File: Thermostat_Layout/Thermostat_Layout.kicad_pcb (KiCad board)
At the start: 2 copper layers, 70 x 60 mm, 52 parts, among them J1 Conn_01x03, J2 Conn_01x02_Male, J3 LCD_HEADER, J4 Conn_Coaxial, J5 Conn_01x04, J6 Conn_01x10, SW1 SW_Push, U1 LM50CIM3, U10 TLP3545, U2 ATMEGA328P-AU, U3 TSR_1-2433, U4 MCP23S17_SO, U5 DS3231MZ, U6 nRF24L01P, U7 FM25V10, U8 TLP3545, U9 TLP3545, Y1 Crystal, Y2 16MHz

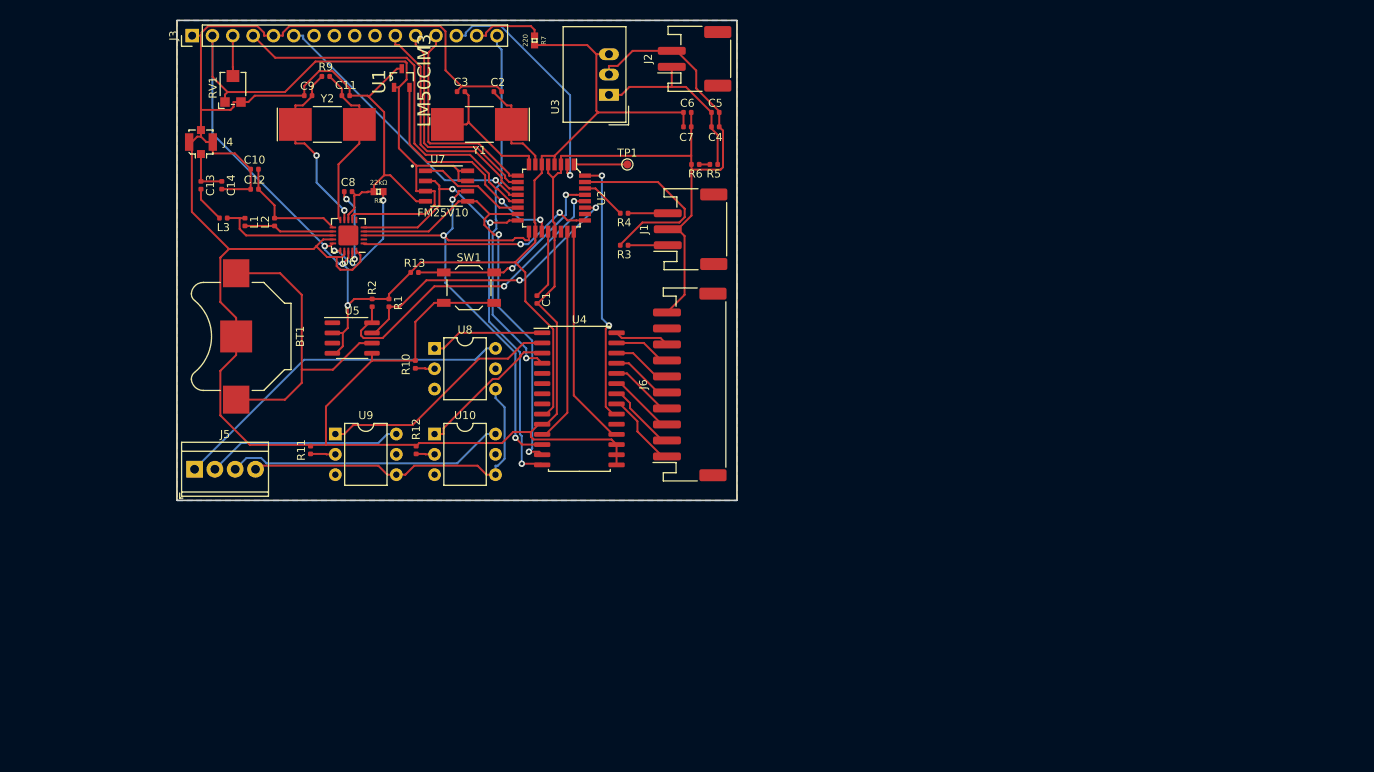
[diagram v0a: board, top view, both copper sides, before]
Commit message: Remove NRF24 from schematic
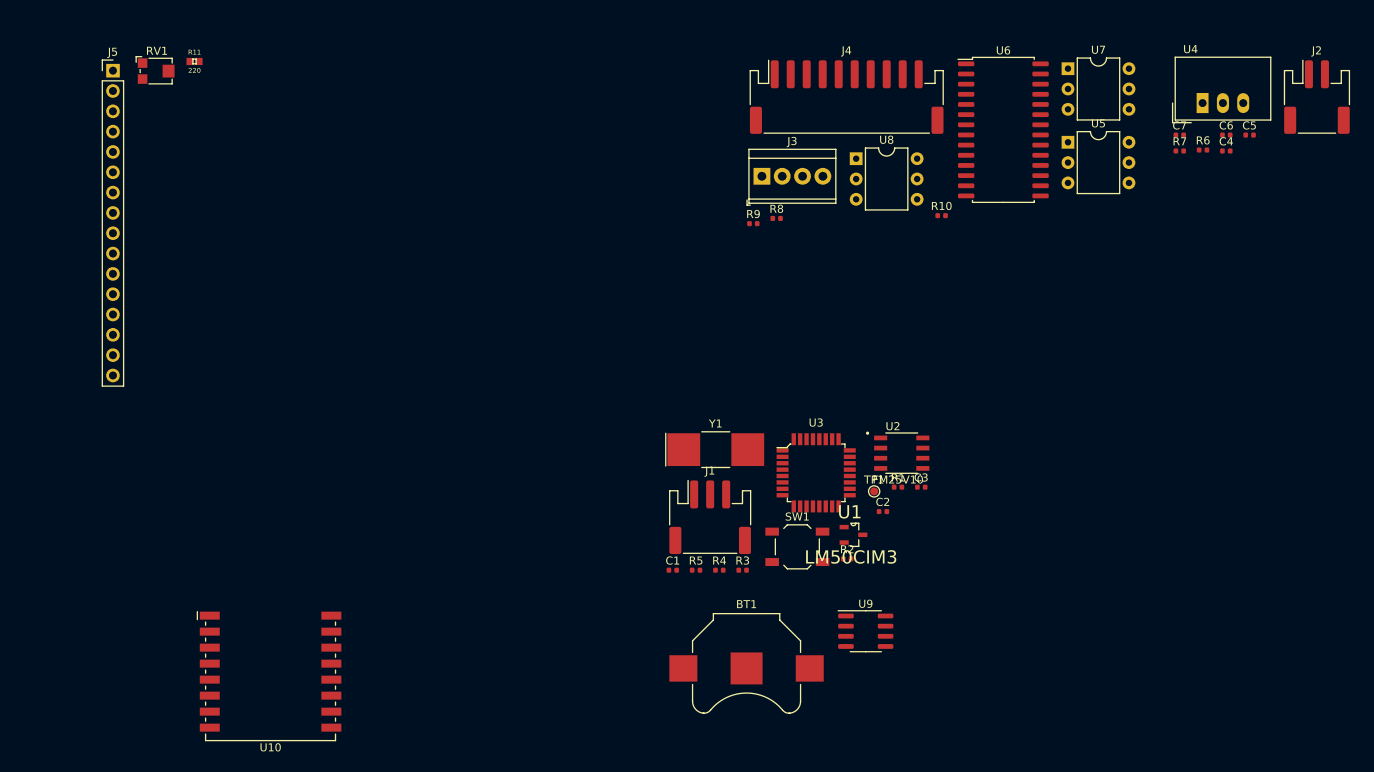
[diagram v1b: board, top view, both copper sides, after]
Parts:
- removed C10: 2.2nF, Capacitor_SMD:C_0402_1005Metric
- removed C11, C9: 22pF, Capacitor_SMD:C_0402_1005Metric
- removed C12: 4.7pF, Capacitor_SMD:C_0402_1005Metric
- removed C13: 15pF, Capacitor_SMD:C_0402_1005Metric
- removed C14: 1.5pF, Capacitor_SMD:C_0402_1005Metric
- removed C8: 33nF, Capacitor_SMD:C_0402_1005Metric
- removed J6: Conn_01x10, Connector_JST:JST_PH_S10B-PH-SM4-TB_1x10-1MP_P2.00mm_Horizontal
- removed L1: 12nH, Inductor_SMD:L_0402_1005Metric
- removed L2: 2.3nH, Inductor_SMD:L_0402_1005Metric
- removed L3: 7.9nH, Inductor_SMD:L_0402_1005Metric
- removed R12: 100Ω, Resistor_SMD:R_0402_1005Metric
- removed R13: 10kΩ, Resistor_SMD:R_0402_1005Metric
- removed Y2: 16MHz, Crystal:Crystal_SMD_SeikoEpson_MC405-2Pin_9.6x4.1mm
- C1: value 100nF -> 22pF
- C3: value 22pF -> 100nF
- J3: value LCD_HEADER -> Conn_01x04; footprint Connector_PinHeader_2.54mm:PinHeader_1x16_P2.54mm_Vertical -> TerminalBlock_TE-Connectivity:TerminalBlock_TE_282834-4_1x04_P2.54mm_Horizontal
- J4: value Conn_Coaxial -> Conn_01x10; footprint Connector_Coaxial:U.FL_Molex_MCRF_73412-0110_Vertical -> Connector_JST:JST_PH_S10B-PH-SM4-TB_1x10-1MP_P2.00mm_Horizontal
- J5: value Conn_01x04 -> LCD_HEADER; footprint TerminalBlock_TE-Connectivity:TerminalBlock_TE_282834-4_1x04_P2.54mm_Horizontal -> Connector_PinHeader_2.54mm:PinHeader_1x16_P2.54mm_Vertical
- R11: value 100Ω -> 220; footprint Resistor_SMD:R_0402_1005Metric -> Resistors:0402
- R3: value 1kΩ -> 10kΩ
- R5: value 220k -> 1kΩ
- R6: value 100k -> 220k
- R7: value 220 -> 100k; footprint Resistors:0402 -> Resistor_SMD:R_0402_1005Metric
- R8: value 22kΩ -> 100Ω; footprint Resistors:0402 -> Resistor_SMD:R_0402_1005Metric
- R9: value 1MΩ -> 100Ω
- U10: value TLP3545 -> ESP-07; footprint Package_DIP:DIP-6_W7.62mm -> RF_Module:ESP-07
- U2: value ATMEGA328P-AU -> FM25V10; footprint digikey-footprints:TQFP-32_7x7mm -> FM25V10:SOIC127P601X172-8N
- U3: value TSR_1-2433 -> ATMEGA328P-AU; footprint Converter_DCDC:Converter_DCDC_TRACO_TSR-1_THT -> digikey-footprints:TQFP-32_7x7mm
- U4: value MCP23S17_SO -> TSR_1-2433; footprint Package_SO:SOIC-28W_7.5x17.9mm_P1.27mm -> Converter_DCDC:Converter_DCDC_TRACO_TSR-1_THT
- U5: value DS3231MZ -> TLP3545; footprint Package_SO:SOIC-8_3.9x4.9mm_P1.27mm -> Package_DIP:DIP-6_W7.62mm
- U6: value nRF24L01P -> MCP23S17_SO; footprint Package_DFN_QFN:QFN-20-1EP_4x4mm_P0.5mm_EP2.5x2.5mm -> Package_SO:SOIC-28W_7.5x17.9mm_P1.27mm
- U7: value FM25V10 -> TLP3545; footprint FM25V10:SOIC127P601X172-8N -> Package_DIP:DIP-6_W7.62mm
- U9: value TLP3545 -> DS3231MZ; footprint Package_DIP:DIP-6_W7.62mm -> Package_SO:SOIC-8_3.9x4.9mm_P1.27mm
- moved U5 92.8 mm to (167.8, 52.9)
- moved U4 86.2 mm to (184.6, 48.0)
- moved U6 82.9 mm to (159.7, 51.4), turned to 0 degrees
- moved R7 81.8 mm to (181.8, 54.0), turned to 0 degrees
- moved J4 80.9 mm to (140.1, 47.3)
- moved U1 80.3 mm to (141.0, 102.0), turned to 0 degrees
- moved U7 79.1 mm to (167.8, 43.7)
- moved J2 77.9 mm to (198.9, 47.3), turned to 0 degrees
- moved BT1 76.1 mm to (127.6, 118.7), turned to 0 degrees
- moved C3 75.9 mm to (149.4, 96.0), turned to 0 degrees
- moved J3 73.4 mm to (129.5, 57.2), turned to 0 degrees
- moved C2 71.2 mm to (144.7, 99.1)
- moved U9 70.7 mm to (142.5, 114.0)
- moved R10 68.4 mm to (152.0, 62.1), turned to 0 degrees
- moved R1 67.7 mm to (146.5, 96.0), turned to 0 degrees
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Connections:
- C1 pad 1: Net-(C1-Pad1) -> /ProcessorConnections/X1
- C2 pad 1: /ProcessorConnections/X1 -> /ProcessorConnections/X2
- C3 pad 1: /ProcessorConnections/X2 -> Net-(C3-Pad1)
- J3 pad 1: GND -> HEAT_HOT
- J3 pad 2: 3.3V -> COOL_HOT
- J3 pad 3: LCD_CONT -> FAN_HOT
- J3 pad 4: LCD_RS -> COMMON
- J4 pad 1: Net-(C13-Pad1) -> UP_BTN
- J4 pad 2: GND -> DWN_BTN
- J5 pad 1: HEAT_HOT -> GND
- J5 pad 2: COOL_HOT -> 3.3V
- J5 pad 3: FAN_HOT -> LCD_CONT
- J5 pad 4: COMMON -> LCD_RS
- R11 pad 1: Net-(R11-Pad1) -> Net-(J5-Pad15)
- R11 pad 2: GND -> 3.3V
- R3 pad 1: Net-(J1-Pad1) -> 3.3V
- R3 pad 2: UC_TX -> UC_RST
- R4 pad 1: Net-(J1-Pad3) -> Net-(J1-Pad1)
- R4 pad 2: UC_RX -> UC_TX
- R5 pad 1: +9V -> Net-(J1-Pad3)
- R5 pad 2: /Power/BATT_MON -> UC_RX
- R6 pad 1: /Power/BATT_MON -> +9V
- R6 pad 2: GND -> /Power/BATT_MON
- R7 pad 1: Net-(J3-Pad15) -> /Power/BATT_MON
- R7 pad 2: 3.3V -> GND
- R9 pad 1: Net-(C11-Pad1) -> Net-(R9-Pad1)
- R9 pad 2: Net-(C9-Pad1) -> GND
- U10 pad 1: FAN_ON -> (no net)
- U10 pad 2: Net-(R12-Pad1) -> (no net)
- U10 pad 4: COMMON -> (no net)
- U10 pad 6: FAN_HOT -> (no net)
- U2 pad 1: Net-(TP1-Pad1) -> MEM_CS
- U2 pad 2: LCD_D7 -> MISO
- U2 pad 3: GND -> 3.3V
- U2 pad 4: 3.3V -> GND
- U2 pad 5: GND -> MOSI
- U2 pad 6: 3.3V -> SCK
- U2 pad 7: /ProcessorConnections/X1 -> 3.3V
- U2 pad 8: /ProcessorConnections/X2 -> 3.3V
- U3 pad 1: +9V -> Net-(TP1-Pad1)
- U3 pad 2: GND -> LCD_D7
- U3 pad 3: 3.3V -> GND
- U4 pad 1: HEAT_ON -> +9V
- U4 pad 2: COOL_ON -> GND
- U4 pad 3: FAN_ON -> 3.3V
- U5 pad 1: (no net) -> HEAT_ON
- U5 pad 2: 3.3V -> Net-(R8-Pad1)
- U5 pad 4: 3.3V -> COMMON
- U5 pad 5: GND -> (no net)
- U5 pad 6: Net-(BT1-Pad1) -> HEAT_HOT
- U6 pad 1: RF_CE -> HEAT_ON
- U6 pad 10: Net-(C11-Pad1) -> GND
- U6 pad 11: Net-(C10-Pad2) -> EXP_CS
- U6 pad 12: Net-(L1-Pad2) -> SCK
- U6 pad 13: Net-(L1-Pad1) -> MOSI
- U6 pad 14: GND -> MISO
- U6 pad 15: 3.3V -> GND
- U6 pad 16: Net-(R8-Pad1) -> GND
- U6 pad 18: 3.3V -> EXP_RST
- U6 pad 19: Net-(C8-Pad1) -> (no net)
- U6 pad 2: (no net) -> COOL_ON
- U6 pad 20: GND -> EXP_INT
- U6 pad 21: (no net) -> UP_BTN
- U6 pad 3: SCK -> FAN_ON
- U6 pad 4: MOSI -> LCD_LED
- U6 pad 5: MISO -> (no net)
- U6 pad 7: 3.3V -> (no net)
- U6 pad 8: GND -> (no net)
- U6 pad 9: Net-(C9-Pad1) -> 3.3V
- U7 pad 1: MEM_CS -> COOL_ON
- U7 pad 2: MISO -> Net-(R9-Pad1)
- U7 pad 3: 3.3V -> (no net)
- U7 pad 4: GND -> COMMON
- U7 pad 5: MOSI -> (no net)
- U7 pad 6: SCK -> COOL_HOT
- U8 pad 1: HEAT_ON -> FAN_ON
- U8 pad 6: HEAT_HOT -> FAN_HOT
- U9 pad 1: COOL_ON -> (no net)
- U9 pad 2: Net-(R11-Pad1) -> 3.3V
- U9 pad 4: COMMON -> 3.3V
- U9 pad 5: (no net) -> GND
- U9 pad 6: COOL_HOT -> Net-(BT1-Pad1)
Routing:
- net GND: track 404.9 -> 0.00 mm
- net 3.3V: track 228.1 -> 0.00 mm, vias 3 -> 0
- net SCK: track 62.4 -> 0.00 mm, vias 3 -> 0
- net MISO: track 61.1 -> 0.00 mm, vias 3 -> 0
- net MOSI: track 56.3 -> 0.00 mm, vias 2 -> 0
- net LCD_RS: track 48.0 -> 0.00 mm
- net LCD_LED: track 45.1 -> 0.00 mm, vias 1 -> 0
- net HEAT_HOT: track 43.9 -> 0.00 mm
- net COMMON: track 43.4 -> 0.00 mm
- net SCL: track 40.7 -> 0.00 mm, vias 2 -> 0
- net Net-(BT1-Pad1): track 39.5 -> 0.00 mm
- net SDA: track 36.8 -> 0.00 mm, vias 2 -> 0
- net LCD_EN: track 36.5 -> 0.00 mm, vias 1 -> 0
- net FAN_HOT: track 34.9 -> 0.00 mm
- net EXP_INT: track 33.3 -> 0.00 mm, vias 2 -> 0
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- removed copper zone on B.Cu, net 3.3V
- removed copper zone on F.Cu, net GND
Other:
- board outline removed
- rule pad_to_mask_clearance: 0.051 -> 0

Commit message: FInalize schematic for thermostat
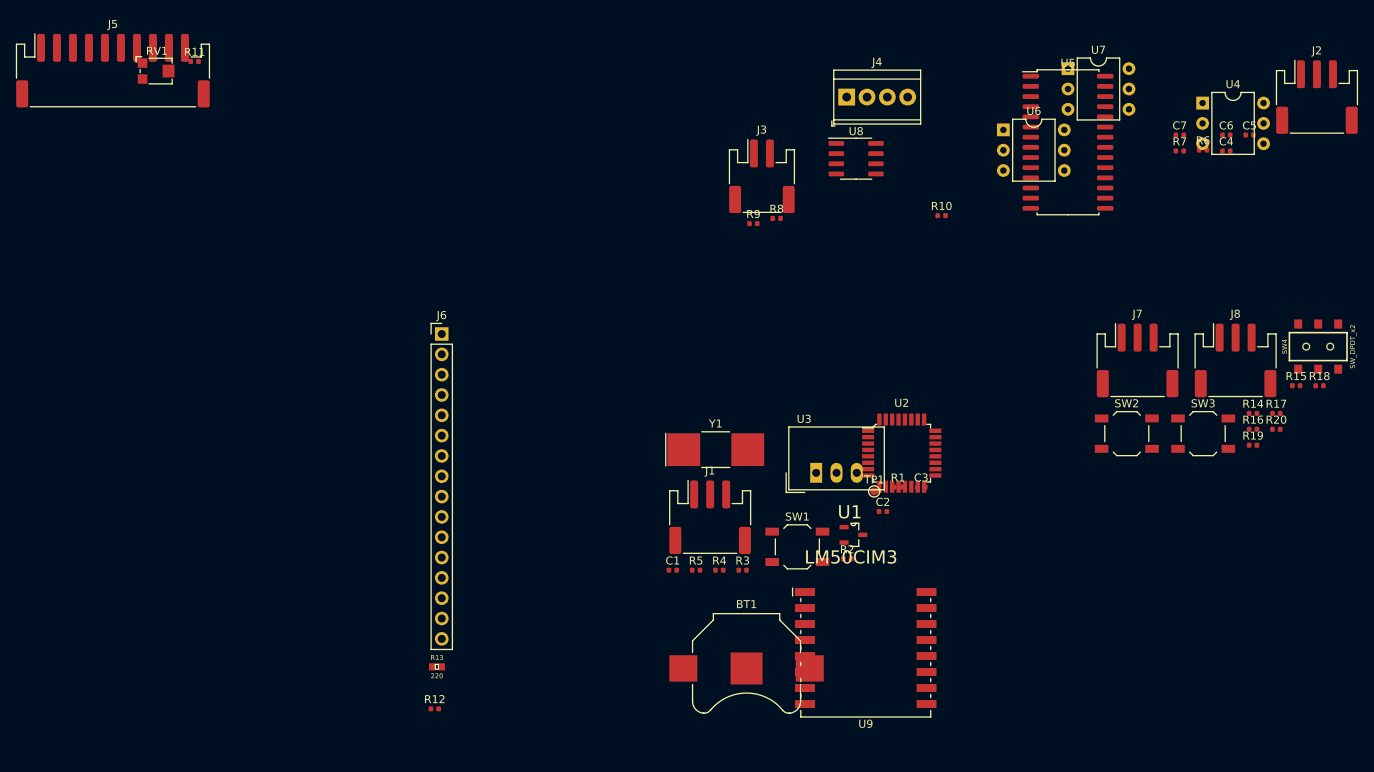
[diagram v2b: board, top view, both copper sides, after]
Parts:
- removed U10: ESP-07, RF_Module:ESP-07
- added J6: LCD_HEADER, Connector_PinHeader_2.54mm:PinHeader_1x16_P2.54mm_Vertical, F.Cu at (89.5, 76.9)
- added J7: Conn_01x03, Connector_JST:JST_PH_S3B-PH-SM4-TB_1x03-1MP_P2.00mm_Horizontal, F.Cu at (176.5, 80.2)
- added J8: Conn_01x03, Connector_JST:JST_PH_S3B-PH-SM4-TB_1x03-1MP_P2.00mm_Horizontal, F.Cu at (188.7, 80.2)
- added R12: 100Ω, Resistor_SMD:R_0402_1005Metric, F.Cu at (88.6, 123.8)
- added R13: 220, Resistors:0402, F.Cu at (88.9, 118.5)
- added R14: 10k, Resistor_SMD:R_0402_1005Metric, F.Cu at (190.9, 86.8)
- added R15: 10k, Resistor_SMD:R_0402_1005Metric, F.Cu at (196.3, 83.4)
- added R16: 1k, Resistor_SMD:R_0402_1005Metric, F.Cu at (190.9, 88.8)
- added R17: 1k, Resistor_SMD:R_0402_1005Metric, F.Cu at (193.8, 86.8)
- added R18: 1k, Resistor_SMD:R_0402_1005Metric, F.Cu at (199.2, 83.4)
- added R19: 1k, Resistor_SMD:R_0402_1005Metric, F.Cu at (190.9, 90.8)
- added R20: 1k, Resistor_SMD:R_0402_1005Metric, F.Cu at (193.8, 88.8)
- added SW2: SW_SPST, Button_Switch_SMD:SW_SPST_TL3342, F.Cu at (175.1, 89.3)
- added SW3: SW_SPST, Button_Switch_SMD:SW_SPST_TL3342, F.Cu at (184.7, 89.3)
- added SW4: SW_DPDT_x2, Switches:SWITCH_DPDT_SMD_AYZ0202, F.Cu at (199.1, 78.5)
- J2: value Conn_01x02_Male -> Conn_01x03; footprint Connector_JST:JST_PH_S2B-PH-SM4-TB_1x02-1MP_P2.00mm_Horizontal -> Connector_JST:JST_PH_S3B-PH-SM4-TB_1x03-1MP_P2.00mm_Horizontal
- J3: value Conn_01x04 -> Conn_01x02_Male; footprint TerminalBlock_TE-Connectivity:TerminalBlock_TE_282834-4_1x04_P2.54mm_Horizontal -> Connector_JST:JST_PH_S2B-PH-SM4-TB_1x02-1MP_P2.00mm_Horizontal
- J4: value Conn_01x10 -> Conn_01x04; footprint Connector_JST:JST_PH_S10B-PH-SM4-TB_1x10-1MP_P2.00mm_Horizontal -> TerminalBlock_TE-Connectivity:TerminalBlock_TE_282834-4_1x04_P2.54mm_Horizontal
- J5: value LCD_HEADER -> Conn_01x10; footprint Connector_PinHeader_2.54mm:PinHeader_1x16_P2.54mm_Vertical -> Connector_JST:JST_PH_S10B-PH-SM4-TB_1x10-1MP_P2.00mm_Horizontal
- R11: value 220 -> 100Ω; footprint Resistors:0402 -> Resistor_SMD:R_0402_1005Metric
- R6: value 220k -> 1kΩ
- R7: value 100k -> 1kΩ
- R8: value 100Ω -> 220k
- R9: value 100Ω -> 100k
- U2: value FM25V10 -> ATMEGA328P-AU; footprint FM25V10:SOIC127P601X172-8N -> digikey-footprints:TQFP-32_7x7mm
- U3: value ATMEGA328P-AU -> TSR_1-2433; footprint digikey-footprints:TQFP-32_7x7mm -> Converter_DCDC:Converter_DCDC_TRACO_TSR-1_THT
- U4: value TSR_1-2433 -> TLP3545; footprint Converter_DCDC:Converter_DCDC_TRACO_TSR-1_THT -> Package_DIP:DIP-6_W7.62mm
- U5: value TLP3545 -> MCP23017_SO; footprint Package_DIP:DIP-6_W7.62mm -> Package_SO:SOIC-28W_7.5x17.9mm_P1.27mm
- U6: value MCP23S17_SO -> TLP3545; footprint Package_SO:SOIC-28W_7.5x17.9mm_P1.27mm -> Package_DIP:DIP-6_W7.62mm
- U8: value TLP3545 -> DS3231MZ; footprint Package_DIP:DIP-6_W7.62mm -> Package_SO:SOIC-8_3.9x4.9mm_P1.27mm
- U9: value DS3231MZ -> ESP-07; footprint Package_SO:SOIC-8_3.9x4.9mm_P1.27mm -> RF_Module:ESP-07
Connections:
- J2 pad 1: +9V -> Net-(J2-Pad1)
- J3 pad 1: HEAT_HOT -> +9V
- J3 pad 2: COOL_HOT -> GND
- J4 pad 1: UP_BTN -> HEAT_HOT
- J4 pad 2: DWN_BTN -> COOL_HOT
- J4 pad 3: MODE_BTN -> FAN_HOT
- J4 pad 4: FAN_BTN -> COMMON
- J5 pad 1: GND -> UP_BTN
- J5 pad 10: (no net) -> GND
- J5 pad 2: 3.3V -> DWN_BTN
- J5 pad 3: LCD_CONT -> MODE_BTN
- J5 pad 4: LCD_RS -> FAN_BTN
- J5 pad 5: GND -> SETTINGS_BTN
- J5 pad 6: LCD_EN -> REMOTE_BTN
- J5 pad 7: (no net) -> SCHED_BTN
- J5 pad 8: (no net) -> UNUSED_BTN
- R11 pad 1: Net-(J5-Pad15) -> Net-(R11-Pad1)
- R11 pad 2: 3.3V -> GND
- R6 pad 1: +9V -> Net-(J2-Pad1)
- R6 pad 2: /Power/BATT_MON -> /ProcessorConnections/DBG_TX
- R7 pad 1: /Power/BATT_MON -> Net-(J2-Pad3)
- R7 pad 2: GND -> /ProcessorConnections/DBG_RX
- R8 pad 1: Net-(R8-Pad1) -> +9V
- R8 pad 2: GND -> /Power/BATT_MON
- R9 pad 1: Net-(R9-Pad1) -> /Power/BATT_MON
- R9 pad 2: GND -> (no net)
- U2 pad 1: MEM_CS -> Net-(TP1-Pad1)
- U2 pad 2: MISO -> LCD_D7
- U2 pad 3: 3.3V -> GND
- U2 pad 4: GND -> 3.3V
- U2 pad 5: MOSI -> GND
- U2 pad 6: SCK -> 3.3V
- U2 pad 7: 3.3V -> /ProcessorConnections/X1
- U2 pad 8: 3.3V -> /ProcessorConnections/X2
- U3 pad 1: Net-(TP1-Pad1) -> +9V
- U3 pad 2: LCD_D7 -> GND
- U3 pad 3: GND -> 3.3V
- U4 pad 1: +9V -> HEAT_ON
- U4 pad 2: GND -> Net-(R10-Pad1)
- U4 pad 3: 3.3V -> (no net)
- U5 pad 2: Net-(R8-Pad1) -> COOL_ON
- U5 pad 3: (no net) -> FAN_ON
- U5 pad 4: COMMON -> LCD_LED
- U5 pad 6: HEAT_HOT -> (no net)
- U6 pad 1: HEAT_ON -> COOL_ON
- U6 pad 2: COOL_ON -> Net-(R11-Pad1)
- U6 pad 3: FAN_ON -> (no net)
- U6 pad 4: LCD_LED -> COMMON
- U6 pad 6: (no net) -> COOL_HOT
- U7 pad 1: COOL_ON -> FAN_ON
- U7 pad 2: Net-(R9-Pad1) -> Net-(R12-Pad1)
- U7 pad 6: COOL_HOT -> FAN_HOT
- U8 pad 1: FAN_ON -> (no net)
- U8 pad 2: Net-(R10-Pad1) -> 3.3V
- U8 pad 4: COMMON -> 3.3V
- U8 pad 5: (no net) -> GND
- U8 pad 6: FAN_HOT -> Net-(BT1-Pad1)
- U9 pad 1: (no net) -> RADIO_RST
- U9 pad 2: 3.3V -> (no net)
- U9 pad 3: (no net) -> RADIO_EN
- U9 pad 4: 3.3V -> (no net)
- U9 pad 5: GND -> /Radio/DBG_RX
- U9 pad 6: Net-(BT1-Pad1) -> /Radio/DBG_TX
- U9 pad 7: SDA -> (no net)
- U9 pad 8: SCL -> 3.3V
